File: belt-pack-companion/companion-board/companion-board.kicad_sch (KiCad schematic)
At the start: 64 parts, among them J1 Conn_01x18_Socket, J2 Conn_01x18_Socket, J4 Conn_01x03_Pin, Q1 MMBT3904, Q2 MMBT3904, U1 TLV320AIC3204, X1 YC24.576MUBCE2O

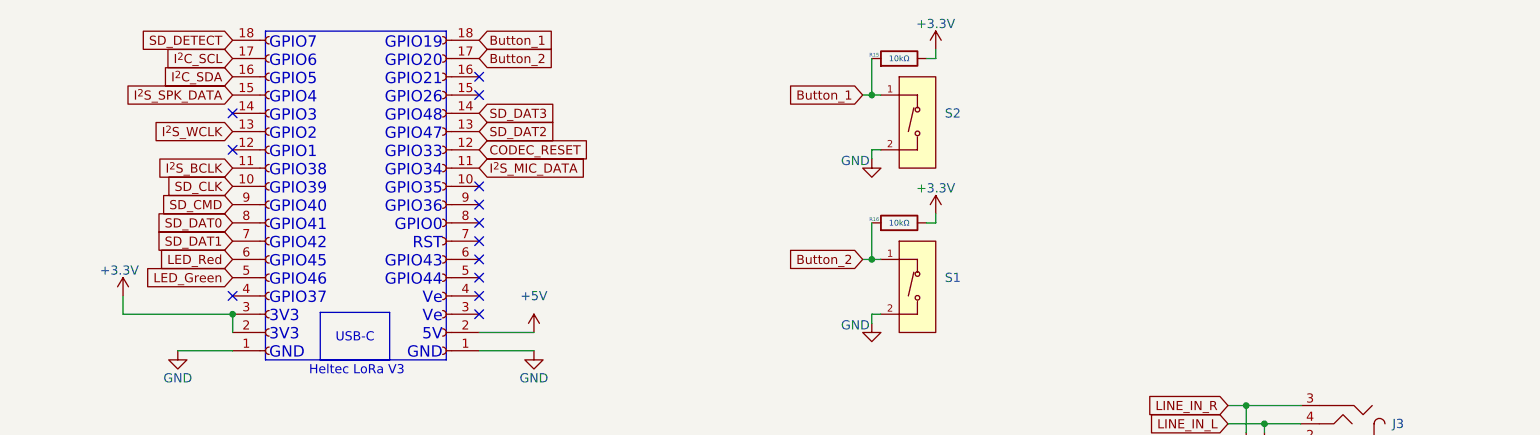
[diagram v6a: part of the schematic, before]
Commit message: Added more GPIO labels and started to add PTT button
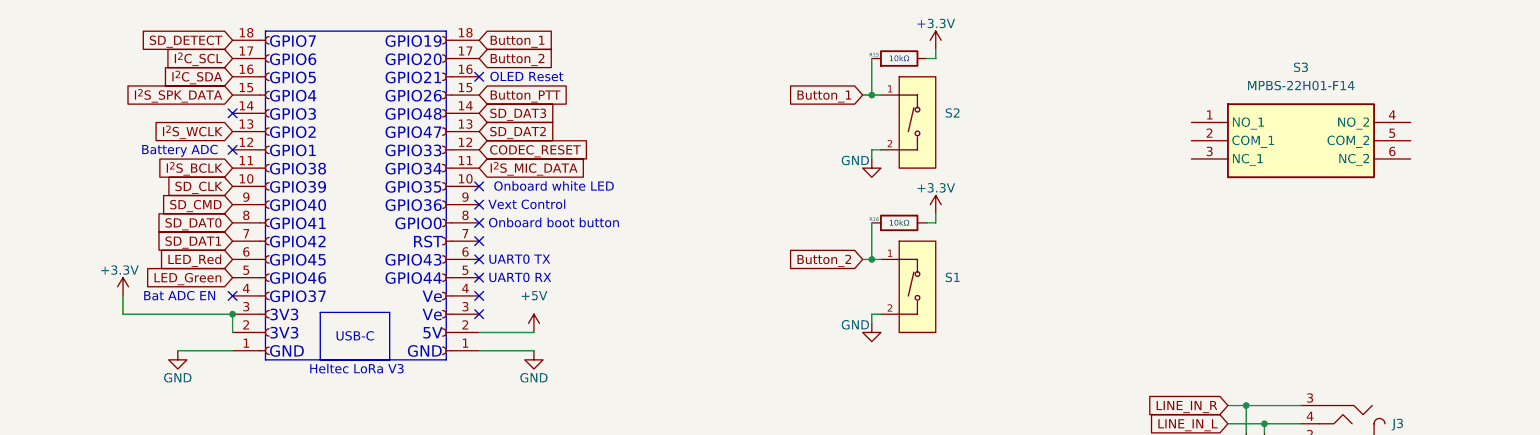
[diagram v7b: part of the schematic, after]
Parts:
- added S3: MPBS-22H01-F14, Footprints:MPBS22H01F14, symbol MPBS-22H01-F14:MPBS-22H01-F14
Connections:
- net Button_PTT: now reaches J2.15 (Pin_15)
- no-connect marks 13 -> 12
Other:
- note added: "Bat ADC EN"
- note added: "Battery ADC"
- note added: "OLED Reset"
- note added: "Onboard boot button"
- note added: "Onboard white LED"
- note added: "UART0 RX"
- note added: "UART0 TX"
- note added: "Vext Control"

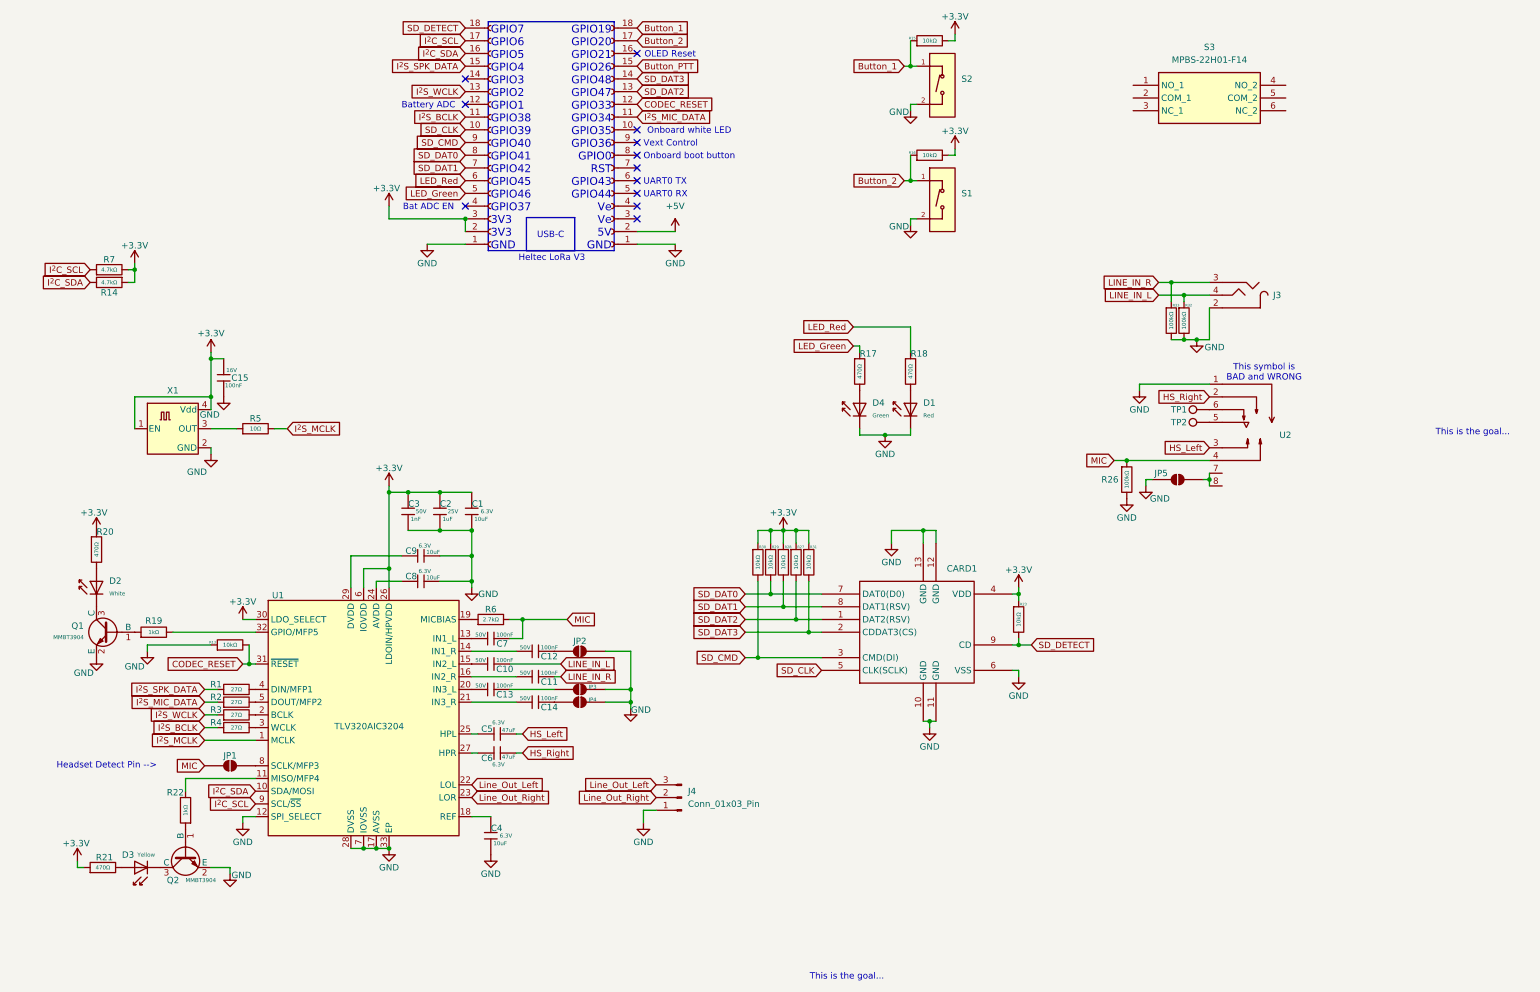
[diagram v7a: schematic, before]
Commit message: Finished laying out components in new layout, ready to route
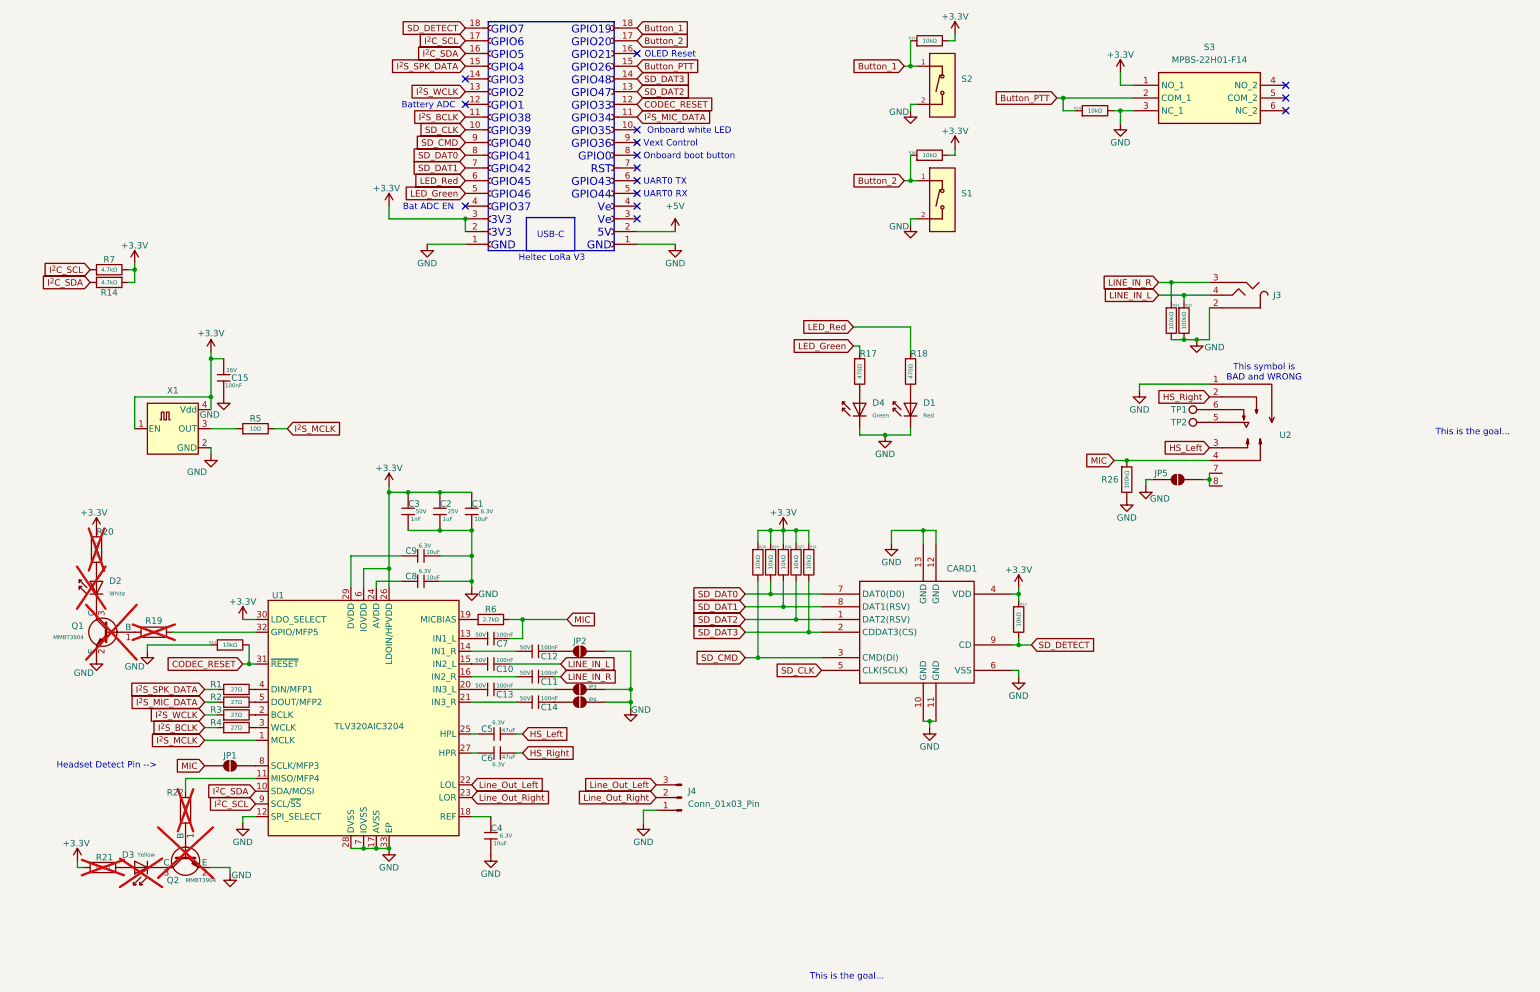
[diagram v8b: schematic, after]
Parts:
- added R24: 10kΩ, PCM_JLCPCB:R_0402, symbol PCM_JLCPCB-Resistors:0402,10kΩ
- D2, D3, Q1, Q2, R19, R20, R21, R22: now not fitted; now left out of the parts list
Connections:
- net +3.3V: now also S3.1 (NO_1)
- net Button_PTT: now also S3.2 (COM_1), R24.1
- net GND: now also S3.3 (NC_1), R24.2
- no-connect marks 12 -> 15
